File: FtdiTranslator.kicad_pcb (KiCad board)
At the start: 2 copper layers, 43.2 x 17.8 mm, 49 parts, among them P1 FTDI-DEVICE, P2 FTDI-HOST, Q1 2N7000, Q2 2N7000, Q3 2N7000, U1 MCP1700

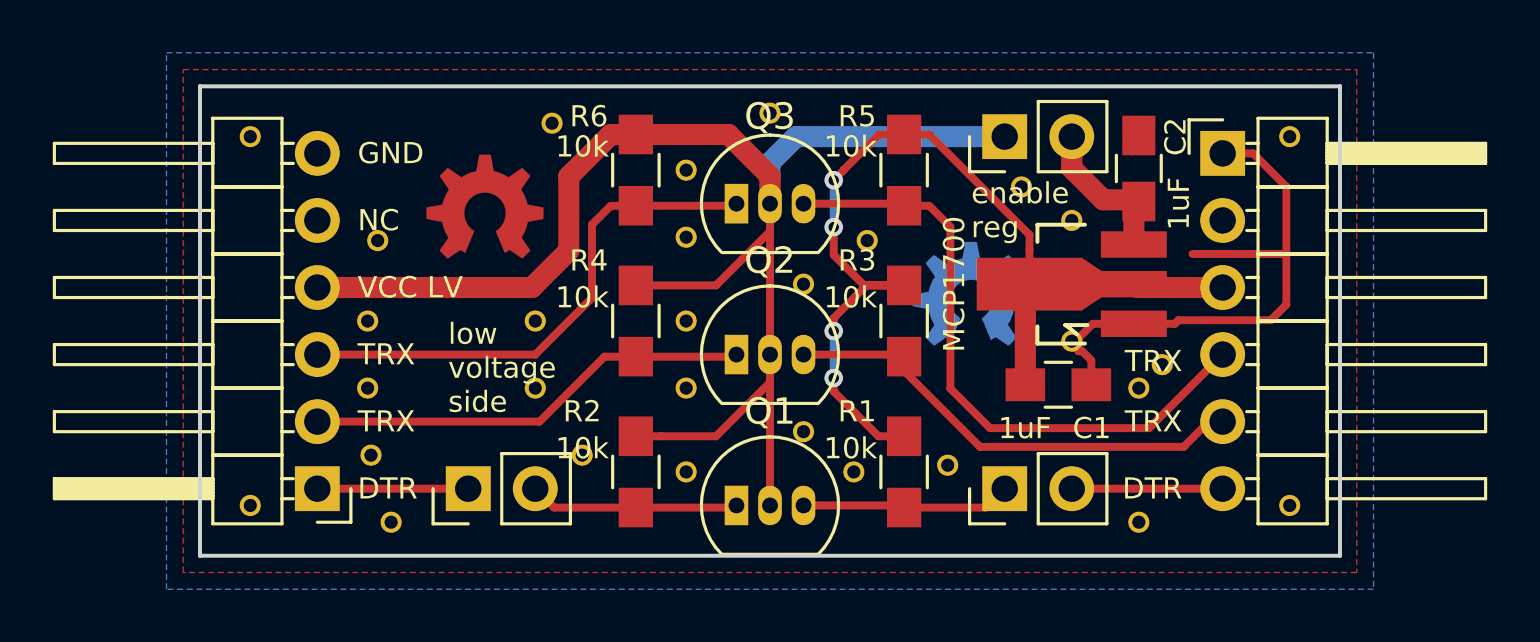
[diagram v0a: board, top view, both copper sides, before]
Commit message: Improve silkscreen readability
This moves some silkscreen text and vias around, and removes some vias
to improve the silkscreen readability.
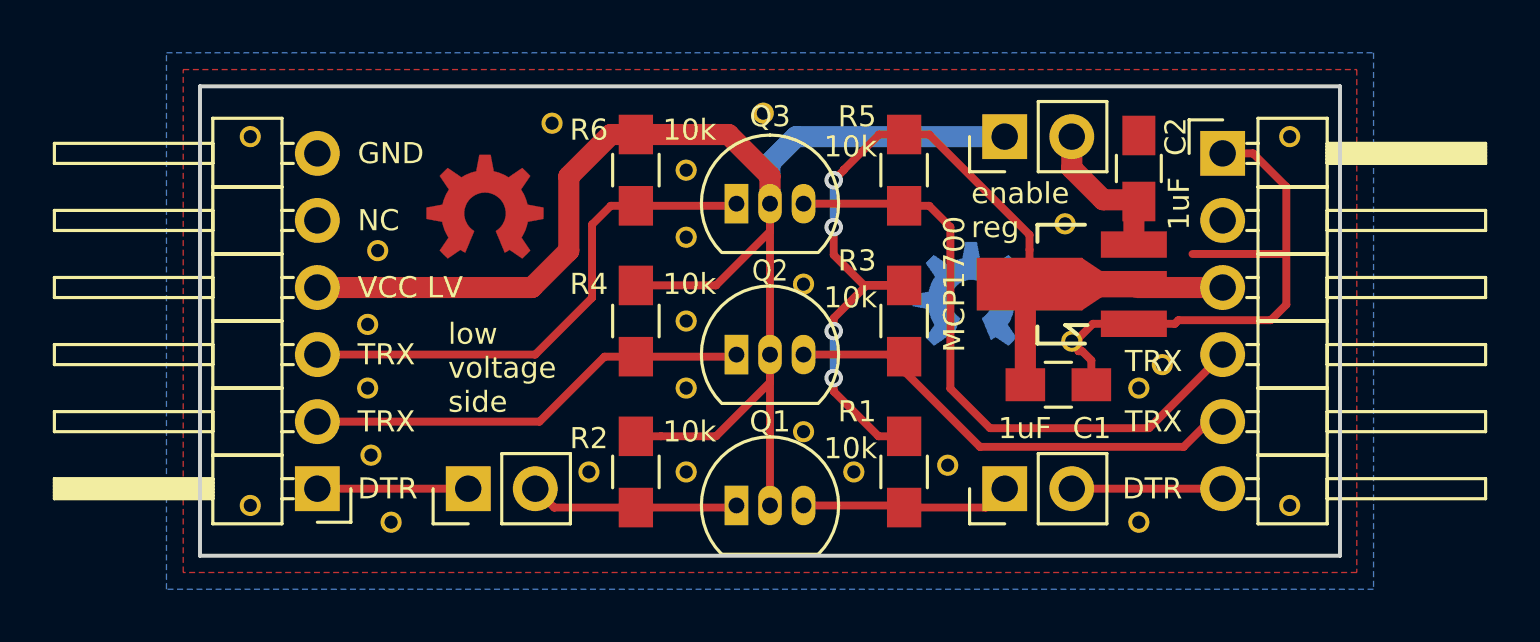
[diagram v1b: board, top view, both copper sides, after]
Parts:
- removed the REF** at (162.6, 98.4)
- removed the REF** at (162.6, 101.0)
- removed the REF** at (175.1, 95.4)
- removed the REF** at (182.9, 94.6)
- moved REF** 2.16 mm to (182.6, 94.7)
- moved REF** 0.68 mm to (164.6, 104.1)
- moved REF** 0.38 mm to (156.6, 95.8)
- moved REF** 0.25 mm to (171.2, 90.6)
- moved REF** 0.13 mm to (156.2, 98.6)
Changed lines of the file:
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@@
     (tracks 115)
     (zones 0)
-    (modules 49)
+    (modules 45)
     (nets 15)
   )
@@
     (35 F.Paste user)
     (36 B.SilkS user)
-    (37 F.SilkS user)
+    (37 F.SilkS user hide)
     (38 B.Mask user)
     (39 F.Mask user)
@@
     (visible_elements FFFFFF7B)
     (pcbplotparams
-      (layerselection 0x00130_80000001)
-      (usegerberextensions false)
+      (layerselection 0x011f0_80000001)
+      (usegerberextensions true)
       (excludeedgelayer true)
       (linewidth 0.100000)
@@
       (drillshape 0)
       (scaleselection 1)
-      (outputdirectory ""))
+      (outputdirectory Gerbers))
   )
   (net 0 "")
@@
   )
   (module Footprints:stitching_via (layer F.Cu)
-    (at 164.338 103.505)
+    (at 164.592 104.14)
     (fp_text reference REF** (at 0 -0.508) (layer F.SilkS) hide
       (effects (font (size 0.127 0.127) (thickness 0.03175)))
@@
   )
   (module Footprints:stitching_via (layer F.Cu)
-    (at 171.45 90.551)
-    (fp_text reference REF** (at 0 -0.508) (layer F.SilkS) hide
-      (effects (font (size 0.127 0.127) (thickness 0.03175)))
-    )
-    (fp_text value via0.8size0.5drill (at 0 -0.762) (layer F.Fab) hide
-      (effects (font (size 0.127 0.127) (thickness 0.03175)))
-    )
-    (pad "" thru_hole circle (at 0 0) (size 0.8 0.8) (drill 0.5) (layers *.Cu)
-      (net 5 GND) (zone_connect 2))
-  )
-  (module Footprints:stitching_via (layer F.Cu)
-    (at 175.133 95.377)
+    (at 171.196 90.551)
     (fp_text reference REF** (at 0 -0.508) (layer F.SilkS) hide
       (effects (font (size 0.127 0.127) (thickness 0.03175)))
@@
   )
   (module Footprints:stitching_via (layer F.Cu)
-    (at 180.975 93.345)
-    (fp_text reference REF** (at 0 -0.508) (layer F.SilkS) hide
-      (effects (font (size 0.127 0.127) (thickness 0.03175)))
-    )
-    (fp_text value via0.8size0.5drill (at 0 -0.762) (layer F.Fab) hide
-      (effects (font (size 0.127 0.127) (thickness 0.03175)))
-    )
-    (pad "" thru_hole circle (at 0 0) (size 0.8 0.8) (drill 0.5) (layers *.Cu)
-      (net 5 GND) (zone_connect 2))
-  )
-  (module Footprints:stitching_via (layer F.Cu)
-    (at 182.88 94.615)
+    (at 182.626 94.742)
     (fp_text reference REF** (at 0 -0.508) (layer F.SilkS) hide
       (effects (font (size 0.127 0.127) (thickness 0.03175)))
@@
   )
   (module Footprints:stitching_via (layer F.Cu)
-    (at 156.21 98.425)
-    (fp_text reference REF** (at 0 -0.508) (layer F.SilkS) hide
-      (effects (font (size 0.127 0.127) (thickness 0.03175)))
-    )
-    (fp_text value via0.8size0.5drill (at 0 -0.762) (layer F.Fab) hide
-      (effects (font (size 0.127 0.127) (thickness 0.03175)))
-    )
-    (pad "" thru_hole circle (at 0 0) (size 0.8 0.8) (drill 0.5) (layers *.Cu)
-      (net 5 GND) (zone_connect 2))
-  )
-  (module Footprints:stitching_via (layer F.Cu)
-    (at 162.56 98.425)
-    (fp_text reference REF** (at 0 -0.508) (layer F.SilkS) hide
-      (effects (font (size 0.127 0.127) (thickness 0.03175)))
-    )
-    (fp_text value via0.8size0.5drill (at 0 -0.762) (layer F.Fab) hide
-      (effects (font (size 0.127 0.127) (thickness 0.03175)))
-    )
-    (pad "" thru_hole circle (at 0 0) (size 0.8 0.8) (drill 0.5) (layers *.Cu)
-      (net 5 GND) (zone_connect 2))
-  )
-  (module Footprints:stitching_via (layer F.Cu)
-    (at 162.56 100.965)
+    (at 156.21 98.552)
     (fp_text reference REF** (at 0 -0.508) (layer F.SilkS) hide
       (effects (font (size 0.127 0.127) (thickness 0.03175)))
@@
   )
   (module Footprints:stitching_via (layer F.Cu)
-    (at 156.591 95.377)
+    (at 156.591 95.758)
     (fp_text reference REF** (at 0 -0.508) (layer F.SilkS) hide
       (effects (font (size 0.127 0.127) (thickness 0.03175)))
@@
     (tags "resistor 0805")
     (attr smd)
-    (fp_text reference R2 (at -2.286 2.032 360) (layer F.SilkS)
+    (fp_text reference R2 (at -1.27 1.778 360) (layer F.SilkS)
       (effects (font (size 0.8 0.8) (thickness 0.15)))
     )
-    (fp_text value 10k (at -0.889 2.032 360) (layer F.SilkS)
+    (fp_text value 10k (at -1.524 -2.032 360) (layer F.SilkS)
       (effects (font (size 0.8 0.8) (thickness 0.15)))
     )
@@
     (tags "resistor 0805")
     (attr smd)
-    (fp_text reference R4 (at -2.286 1.778 360) (layer F.SilkS)
+    (fp_text reference R4 (at -1.397 1.778 360) (layer F.SilkS)
       (effects (font (size 0.8 0.8) (thickness 0.15)))
     )
-    (fp_text value 10k (at -0.889 2.032 360) (layer F.SilkS)
+    (fp_text value 10k (at -1.397 -2.032 360) (layer F.SilkS)
       (effects (font (size 0.8 0.8) (thickness 0.15)))
     )
@@
     (tags "resistor 0805")
     (attr smd)
-    (fp_text reference R6 (at -2.032 1.778 360) (layer F.SilkS)
+    (fp_text reference R6 (at -1.524 1.778 360) (layer F.SilkS)
       (effects (font (size 0.8 0.8) (thickness 0.15)))
     )
-    (fp_text value 10k (at -0.889 2.032 360) (layer F.SilkS)
+    (fp_text value 10k (at -1.524 -2.032 360) (layer F.SilkS)
       (effects (font (size 0.8 0.8) (thickness 0.15)))
     )
@@
     (tags "to-92 sc-43 sc-43a sot54 PA33 transistor")
     (fp_text reference Q3 (at 1.27 -3.302) (layer F.SilkS)
-      (effects (font (size 1 1) (thickness 0.15)))
+      (effects (font (size 0.8 0.8) (thickness 0.15)))
     )
     (fp_text value 2N7000 (at 1.27 2.79) (layer F.Fab)
@@
     (descr "TO-92 leads in-line, narrow, oval pads, drill 0.6mm (see NXP sot054_po.pdf)")
     (tags "to-92 sc-43 sc-43a sot54 PA33 transistor")
-    (fp_text reference Q2 (at 1.27 -3.56) (layer F.SilkS)
-      (effects (font (size 1 1) (thickness 0.15)))
+    (fp_text reference Q2 (at 1.27 -3.175) (layer F.SilkS)
+      (effects (font (size 0.8 0.7) (thickness 0.15)))
     )
     (fp_text value 2N7000 (at 1.27 2.79) (layer F.Fab)
@@
     (descr "TO-92 leads in-line, narrow, oval pads, drill 0.6mm (see NXP sot054_po.pdf)")
     (tags "to-92 sc-43 sc-43a sot54 PA33 transistor")
-    (fp_text reference Q1 (at 1.27 -3.56) (layer F.SilkS)
-      (effects (font (size 1 1) (thickness 0.15)))
+    (fp_text reference Q1 (at 1.27 -3.175) (layer F.SilkS)
+      (effects (font (size 0.8 0.8) (thickness 0.15)))
     )
     (fp_text value 2N7000 (at 1.27 2.79) (layer F.Fab)
